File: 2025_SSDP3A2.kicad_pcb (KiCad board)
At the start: 4 copper layers, 58.4 x 28.8 mm, 61 parts, among them J1 SolderPad, J2 SolderPad, J3 SolderPad, J4 SolderPad, Q1 IAUZ30N10S5L240, Q2 BSZ096N10LS5, U1 LM5146RGYR

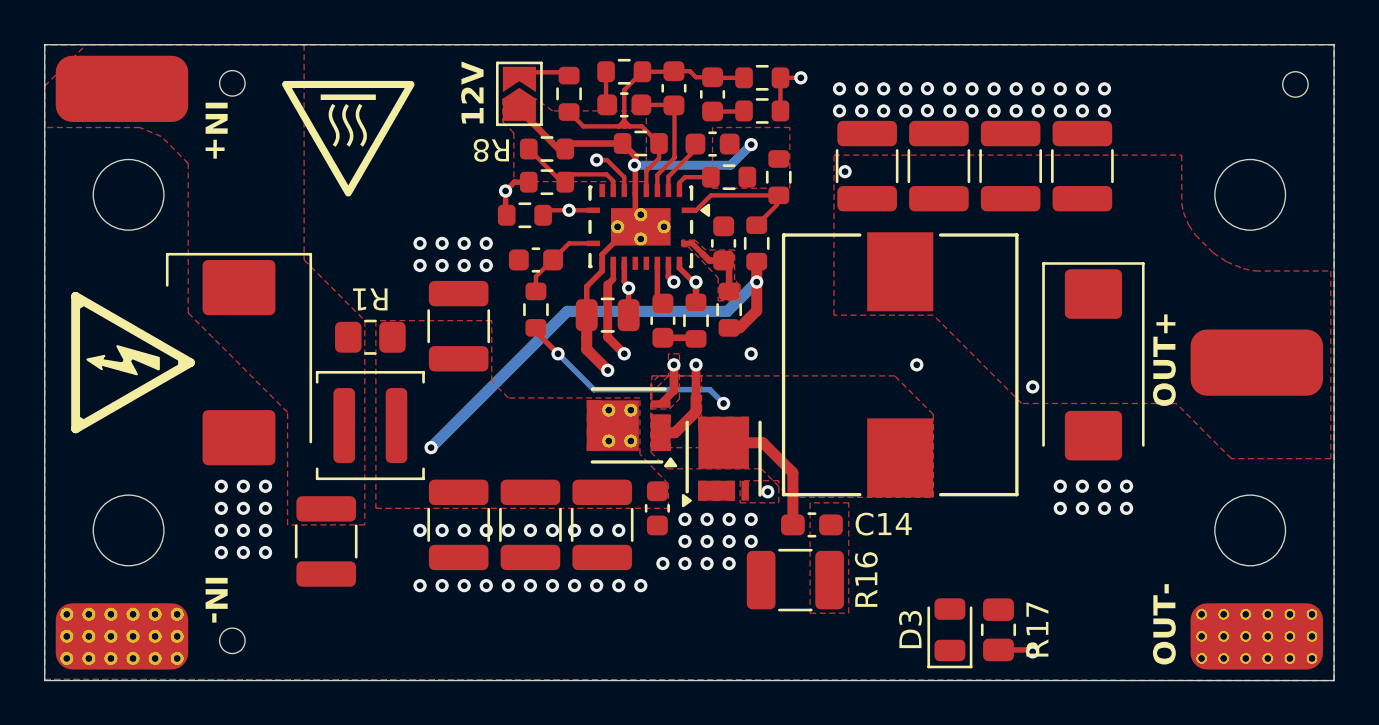
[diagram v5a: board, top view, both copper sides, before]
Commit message: Tweaked feedback routing and removed EMI filter
The EMI filter places an inductor in between the battery and the buck
converter, creating the risk of resonance either at the buck converter
input or on the battery line. While the former issue has been *somewhat*
addressed with the parallel damping resistor, the latter issue cannot be
reasonably fixed without good knowledge of the other various loads that
may be attached to the battery line. For this reason, the EMI filter is
removed.
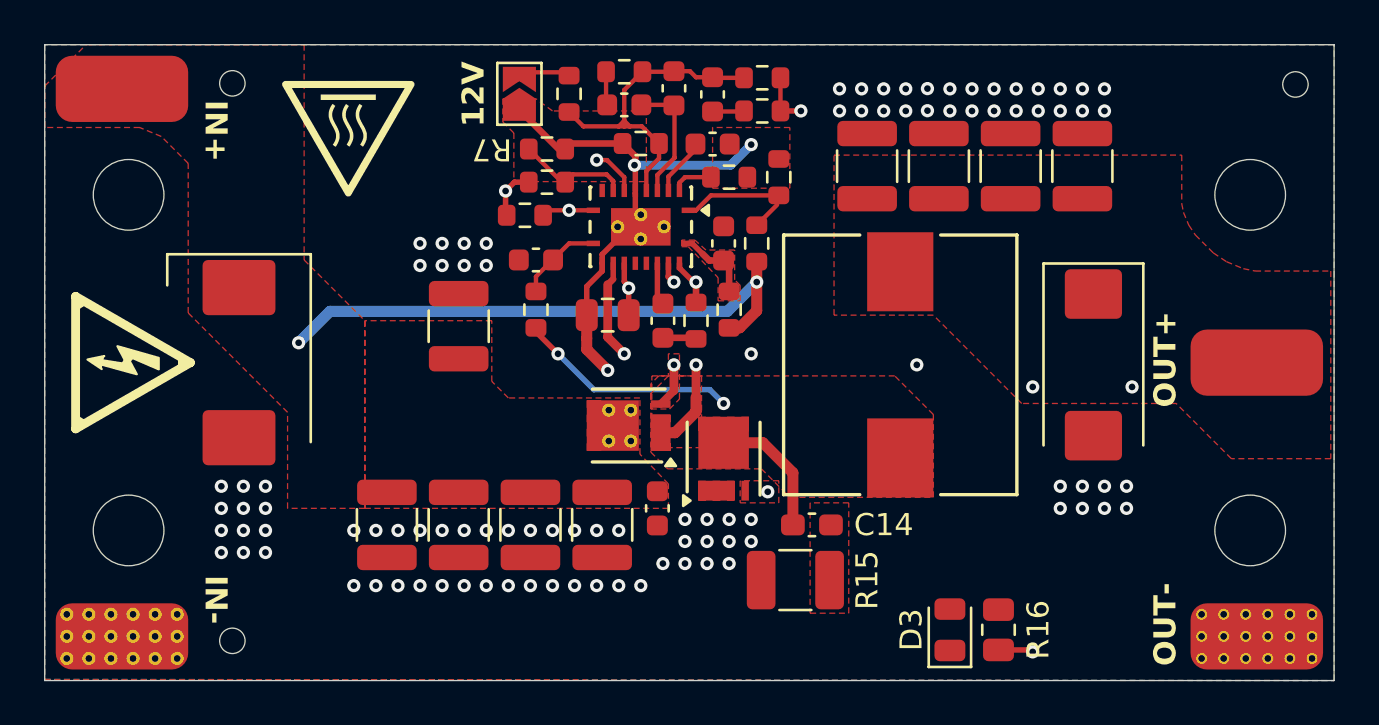
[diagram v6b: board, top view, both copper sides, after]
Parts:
- removed the L1 at (134.8, 117.2)
- removed the R1 at (134.8, 113.2)
- moved C6 2.85 mm to (135.5, 121.8)
- renumbered L2 to L1, R2 to R1, R11 to R10, R12 to R11, R13 to R12, R14 to R13, R15 to R14, R16 to R15, R17 to R16, R3 to R2, R4 to R3, R5 to R4, R6 to R5, R7 to R6, R8 to R7, R9 to R8, R10 to R9
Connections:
- C1 pad 1: VIN -> VBAT
- C2 pad 1: VIN -> VBAT
- C3 pad 1: VIN -> VBAT
- C4 pad 1: VIN -> VBAT
- C5 pad 1: VIN -> VBAT
- Q1 pad 5: VIN -> VBAT
- Q1 pad 6: VIN -> VBAT
- Q1 pad 7: VIN -> VBAT
- Q1 pad 8: VIN -> VBAT
- R1 pad 1: VIN -> VBAT
- R2 pad 1: VIN -> VBAT
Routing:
- net VBAT: track 0.00 -> 25.7 mm, vias 0 -> 2
- net VIN: track 21.7 -> 0.00 mm, vias 2 -> 0
- net VOUT: track 21.0 -> 36.1 mm
- net PGND: vias 90 -> 96
- removed copper zone on F.Cu, net VIN

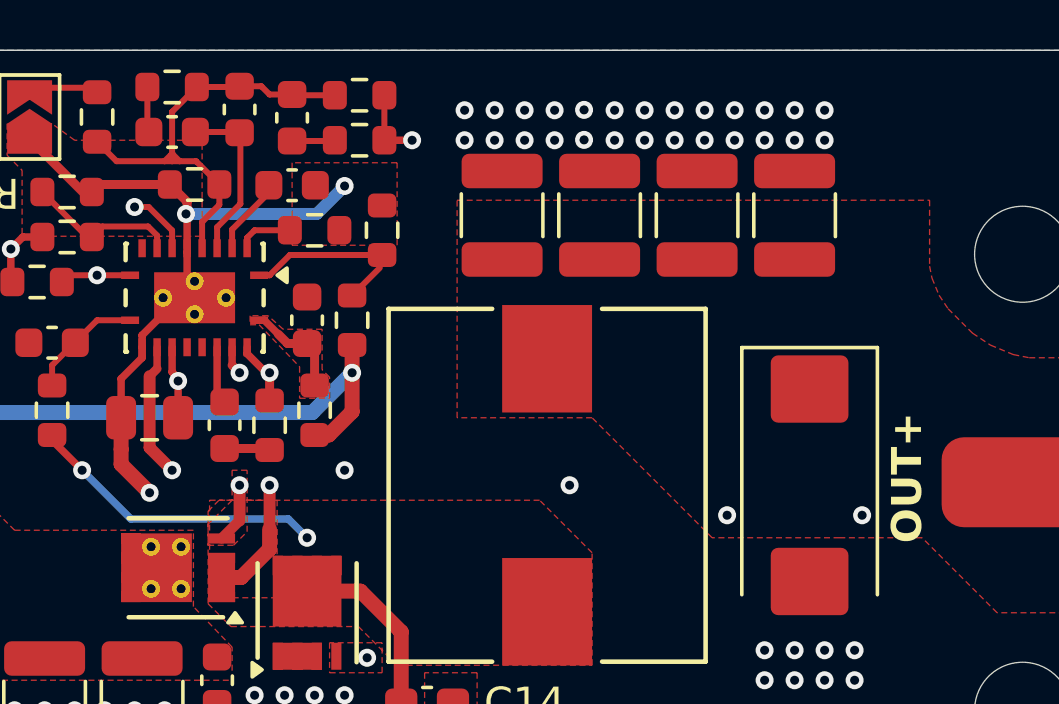
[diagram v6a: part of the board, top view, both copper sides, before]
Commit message: Tweaked routing layers
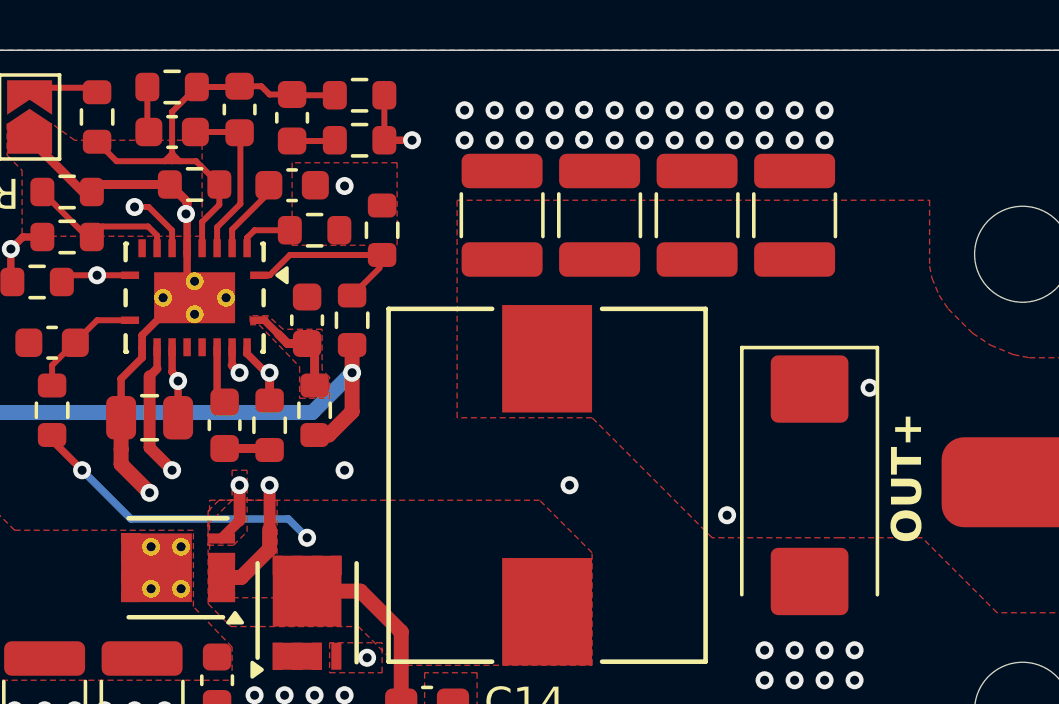
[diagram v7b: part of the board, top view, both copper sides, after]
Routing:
- net VOUT: track 36.1 -> 34.6 mm
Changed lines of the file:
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@@
 		(end 151.068329 105.456671)
 		(width 0.4)
-		(layer "B.Cu")
+		(layer "In2.Cu")
 		(net 2)
 	)
@@
 		(end 152 104.525)
 		(width 0.4)
-		(layer "B.Cu")
+		(layer "In2.Cu")
 		(net 2)
 	)
@@
 	)
 	(via
-		(at 169.25 115.5)
+		(at 169.5 111.25)
 		(size 0.6)
 		(drill 0.3)
@@
 		(drill 0.3)
 		(layers "F.Cu" "B.Cu")
+		(net 11)
+	)
+	(segment
+		(start 169.5 111.25)
+		(end 162.5 111.25)
+		(width 0.25)
+		(layer "In2.Cu")
+		(net 11)
+	)
+	(segment
+		(start 162.5 111.25)
+		(end 154.25 103)
+		(width 0.25)
+		(layer "In2.Cu")
 		(net 11)
 	)
@@
 		(width 0.25)
 		(layer "In2.Cu")
-		(net 11)
-	)
-	(segment
-		(start 154.25 103)
-		(end 166.75 115.5)
-		(width 0.25)
-		(layer "In2.Cu")
-		(net 11)
-	)
-	(segment
-		(start 166.75 115.5)
-		(end 169.25 115.5)
-		(width 0.25)
-		(layer "In2.Cu")

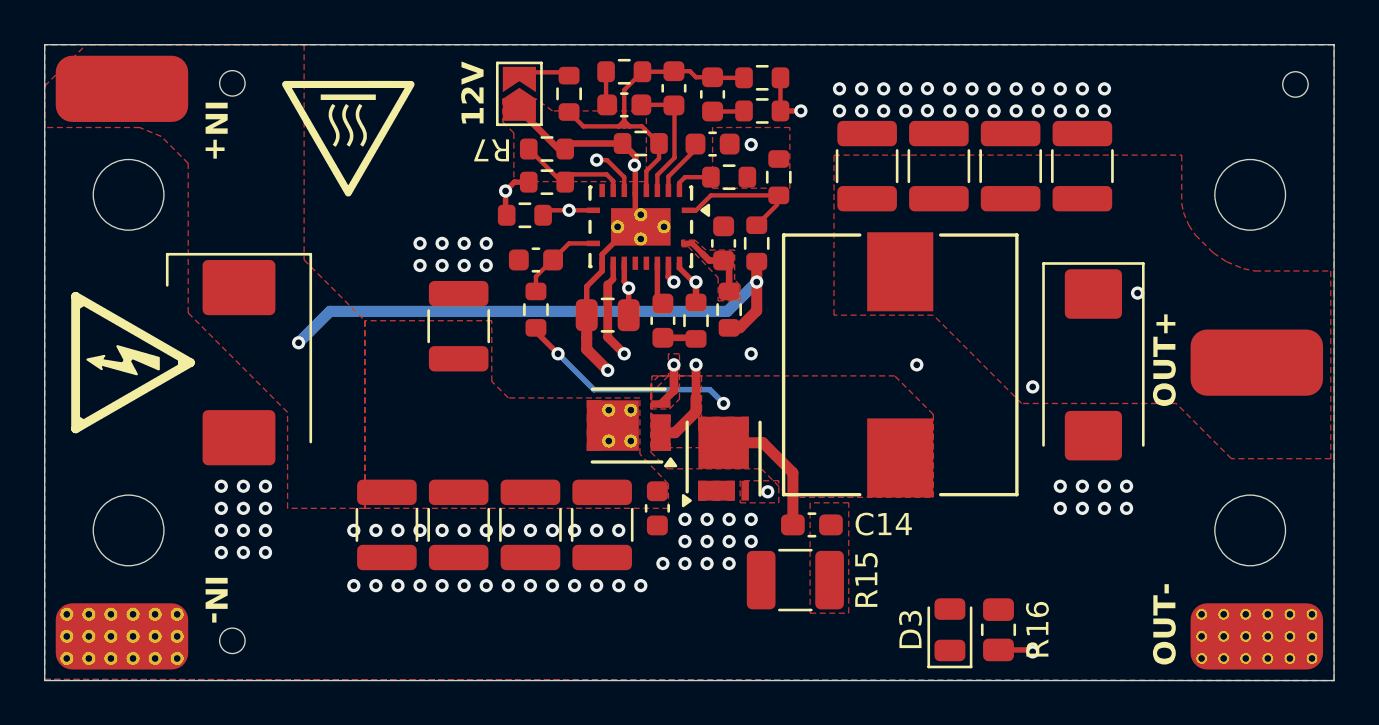
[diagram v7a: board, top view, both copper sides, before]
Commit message: Tweaked routing, added breakout pads, via clean up
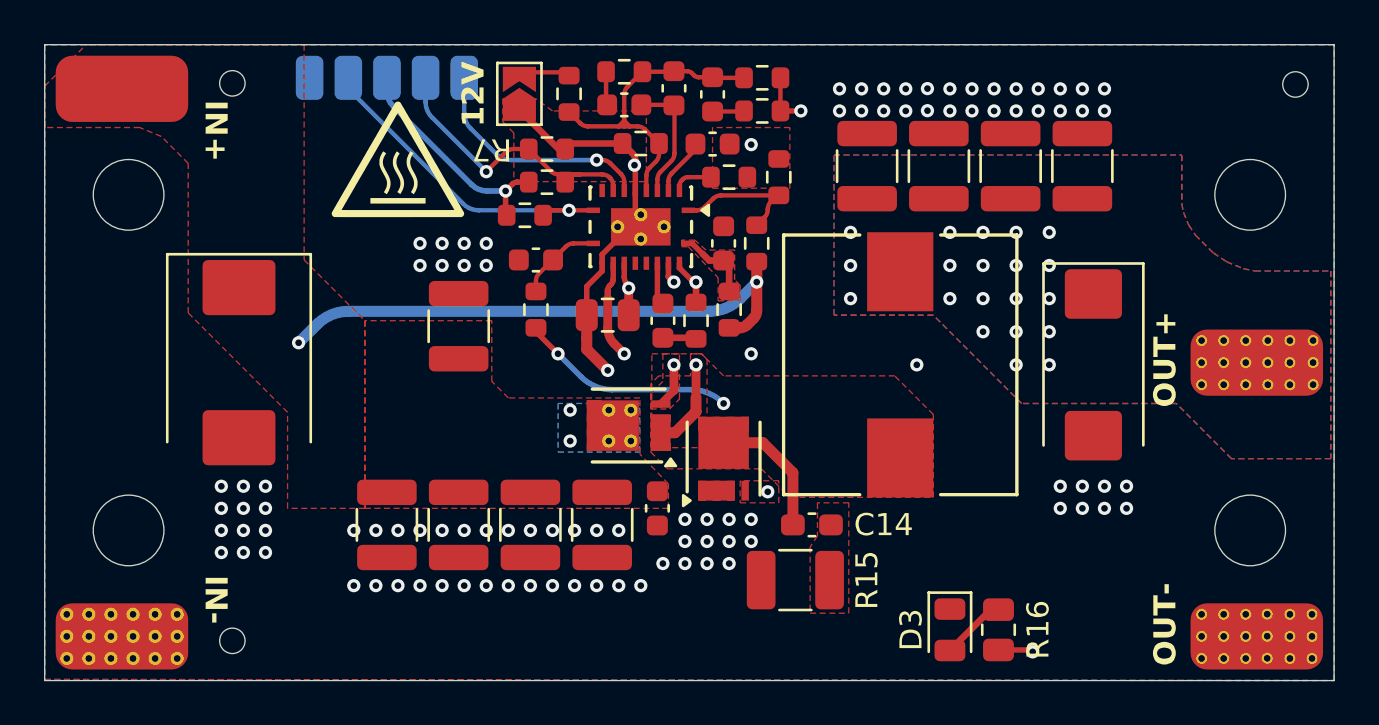
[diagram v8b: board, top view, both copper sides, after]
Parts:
- removed REF** (x2): Symbol_HighVoltage_Triangle_6x6mm_Copper, Symbol:Symbol_HighVoltage_Triangle_6x6mm_Copper
- added J5: SolderPad_01x05, Connector_Custom:SolderWirePad_1x05_SMD_1.5x2mm, B.Cu at (139.2, 101.5)
- moved G*** 20.3 mm to (167.0, 123.0), turned to 180 degrees
- moved G*** 2.44 mm to (136.0, 105.2), turned to 0 degrees
- turned D3 to -90 degrees
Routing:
- net PG: track 2.37 -> 14.8 mm
- net SYNCOUT: track 2.17 -> 10.5 mm
- net SYNCIN: track 4.99 -> 13.0 mm, vias 0 -> 1
- net VCC: track 12.2 -> 19.9 mm
- net VOUT: track 34.6 -> 39.7 mm, vias 4 -> 22
- net /VOUT_LED: track 0.00 -> 2.97 mm
- net VBAT: track 25.7 -> 25.6 mm, vias 2 -> 4
- added copper zone on B.Cu, net VBAT
- added copper zone on In1.Cu, net VBAT
- added copper zone on In2.Cu, net VBAT
- added copper zone on B.Cu, net VOUT
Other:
- board text added: "CAUTION HOT SURFACE"
- board text added: "GND"
- board text added: "PG"
- board text added: "SYNC_I"
- board text added: "SYNC_O"
- board text added: "VCC"
